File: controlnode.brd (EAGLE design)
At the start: 100 x 50 mm, 29 parts, among them J1 ATX24RH, X1 5566-4, X2 5566-6

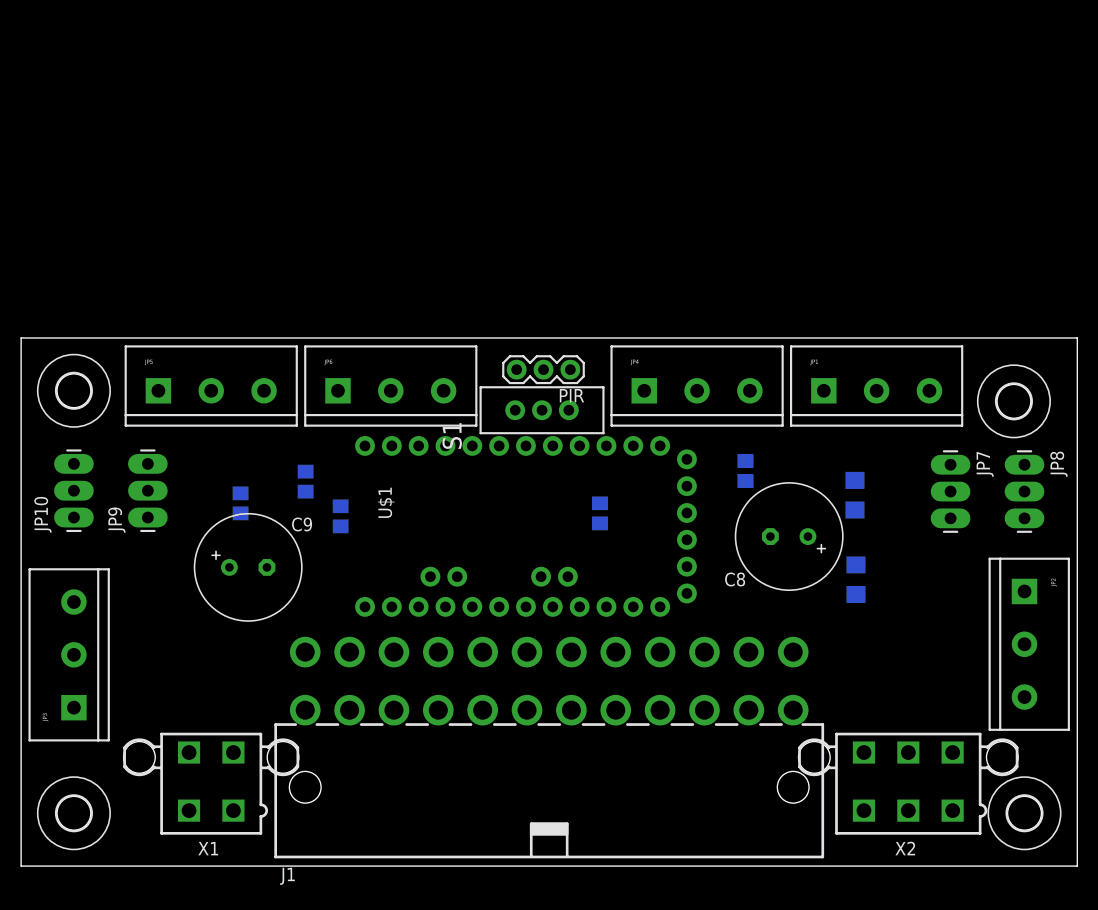
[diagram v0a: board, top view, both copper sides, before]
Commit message: Started working on powernode. Separated controlnode into an own module.
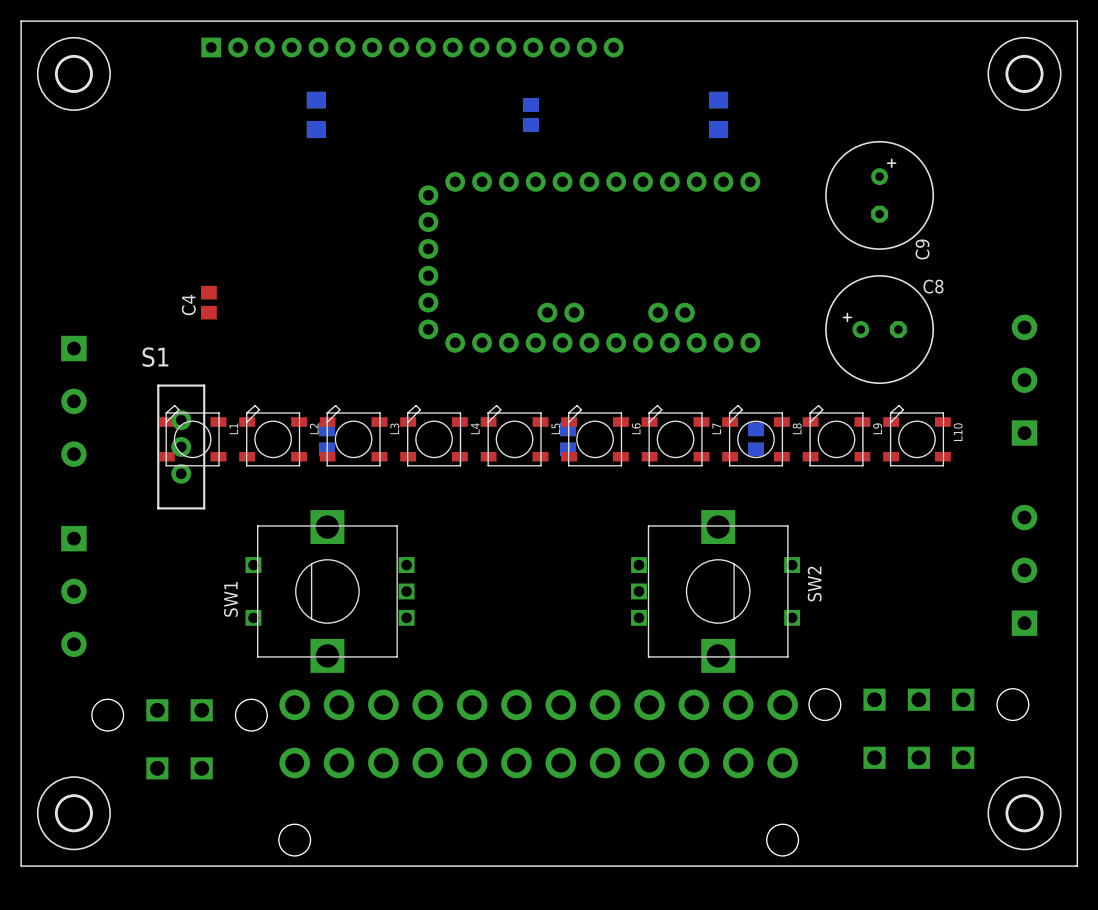
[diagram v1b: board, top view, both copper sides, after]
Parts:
- removed JP10, JP7, JP8, JP9: (no value), SparkFun-Connectors:1X03_LONGPADS
- removed JP5, JP6: (no value), SparkFun-Connectors:SCREWTERMINAL-5MM-3
- removed PIR: (no value), SparkFun-Connectors:1X03
- added L1, L10, L2, L3, L4, L5, L6, L7, L8, L9: WS2812B, adafruit:WS2812B
- added SW1, SW2: EC12E_SW, switch-alps:ALPS_EC12E_SW
- added U1: LCD-16X2NOHOLES, SparkFun:LCD-16X2_NOHOLES
- moved C9 69.4 mm to (81.3, 63.5), turned to 270 degrees
- moved C7 62.4 mm to (27.9, 71.1)
- moved JP4 55.8 mm to (5.00, 31.0), flipped to the bottom, turned to 270 degrees
- moved C6 45.9 mm to (66.0, 71.1)
- moved C5 42.0 mm to (48.3, 71.1)
- moved S1 34.3 mm to (15.2, 39.7), turned to 0 degrees
- moved JP3 34.0 mm to (5.00, 49.0), flipped to the bottom, turned to 270 degrees
- moved H2 31.0 mm to (95.0, 75.0)
- moved H1 30.0 mm to (5.00, 75.0)
- moved U$1 25.7 mm to (53.8, 57.2), flipped to the bottom
- moved C8 21.4 mm to (81.3, 50.8), turned to 0 degrees
- moved JP1 19.4 mm to (95.0, 41.0), flipped to the bottom, turned to 90 degrees
- moved C4 19.2 mm to (17.8, 53.3), flipped to the top
- moved C2 7.62 mm to (51.8, 40.4)
- moved J1 5.10 mm to (49.0, 5.00), flipped to the bottom
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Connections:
- removed net +5V/2: J1.9, PIR.3, U$1.21
- removed net PROXIMITY: PIR.2
- new net 5V_STANDBY: J1.9
- new net N$1: L1.2-DOUT, L2.4-DIN
- new net N$10: L1.4-DIN, U$1.15
- new net N$2: L2.2-DOUT, L3.4-DIN
- new net N$20: U$1.6, U1.15
- new net N$3: L3.2-DOUT, L4.4-DIN
- new net N$4: L4.2-DOUT, L5.4-DIN
- new net N$5: L5.2-DOUT, L6.4-DIN
- new net N$6: L6.2-DOUT, L7.4-DIN
- new net N$7: L7.2-DOUT, L8.4-DIN
- new net N$8: L8.2-DOUT, L9.4-DIN
- new net N$9: L10.4-DIN, L9.2-DOUT
- new net VDD: U1.2
- new net VSS: U1.1
- net +5V: now also L1.1-VDD, L10.1-VDD, L2.1-VDD, L3.1-VDD, L4.1-VDD, L5.1-VDD, L6.1-VDD, L7.1-VDD, L8.1-VDD, L9.1-VDD, U$1.21
- net GND: now also L1.3-GND, L10.3-GND, L2.3-GND, L3.3-GND, L4.3-GND, L5.3-GND, L6.3-GND, L7.3-GND, L8.3-GND, L9.3-GND, U1.16; no longer PIR.1, U$1.23
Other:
- board size 100 x 50 mm -> 100 x 80 mm
